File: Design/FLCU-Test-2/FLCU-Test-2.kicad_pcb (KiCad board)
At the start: 2 copper layers, 69.1 x 46.2 mm, 57 parts, among them J1 ICSP, J2 UART, J3 0348260124, U1 ATmega328-AU, U2 ULN2003ADR, U3 MCP2515-xST, U4 TJR1443, U5 NCV4276B, Y1 CSTNE16M0V530000R0, Y2 8MHz

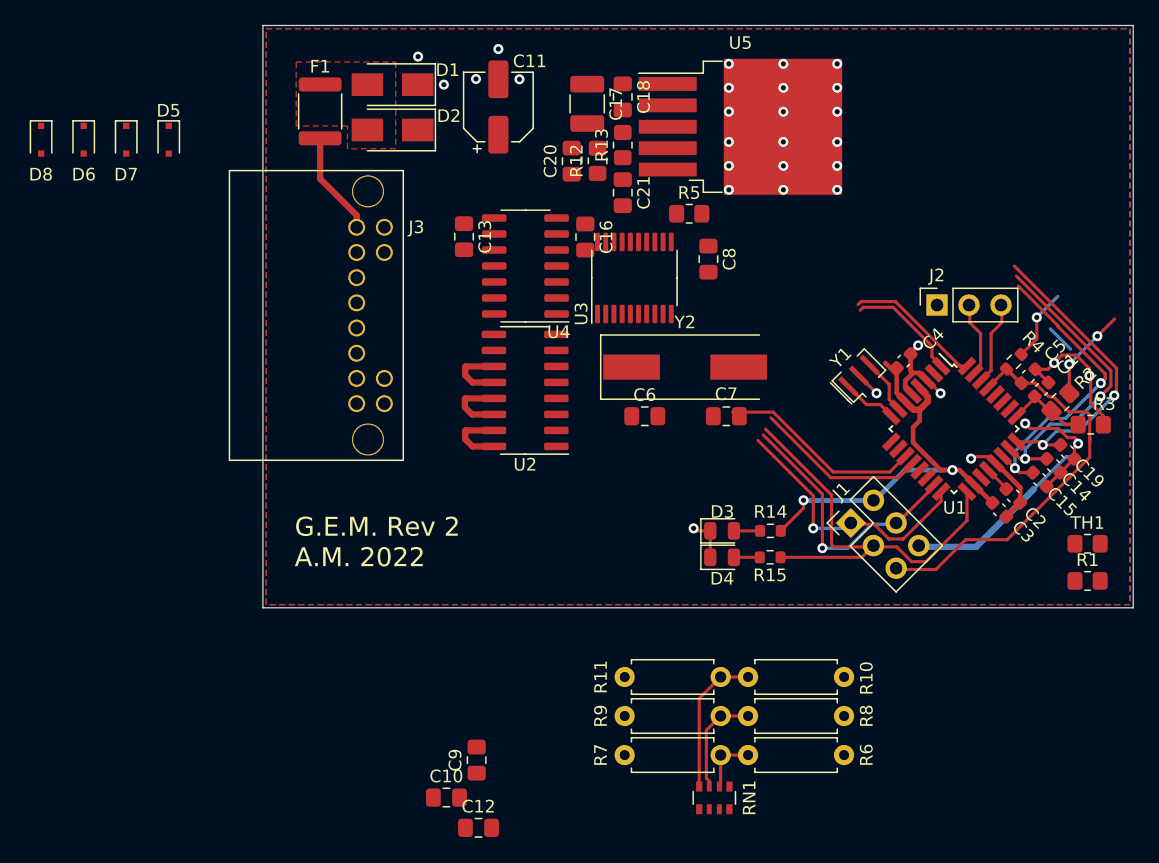
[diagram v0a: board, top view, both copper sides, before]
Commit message: Tentative Completion of Rev2 of FLCU / GEM  - Switch to TJR1443 CAN transceiver  - Smaller, more modern crystal for MCP2515  - Pulse-forming network to use sleep/wake functionality of TJR1443  - Switch from 12 to 16 pin connector to allow one additional analog input,    one digital pulse capture input, +5VOUT and signal ground  - Put CAN INT on an actual interrupt pin (lol)
This revision was done to correct some sleep/wake issues with Rev1, and to support it's use as a boost controller (with different FW)

 - Out - PWM Boost Control Solenoid
 - Out - PWM Electric Water Pump (Intercooler)
 - Out - Intercooler Fan Relay
 - DIn - Turbine speed
 - AIn - Manifold Pressure
 - AIn - Discharge Air Temperature
 - AIn - Intercooler Water Temperature
 - AIn - There was one more that I'm forgetting
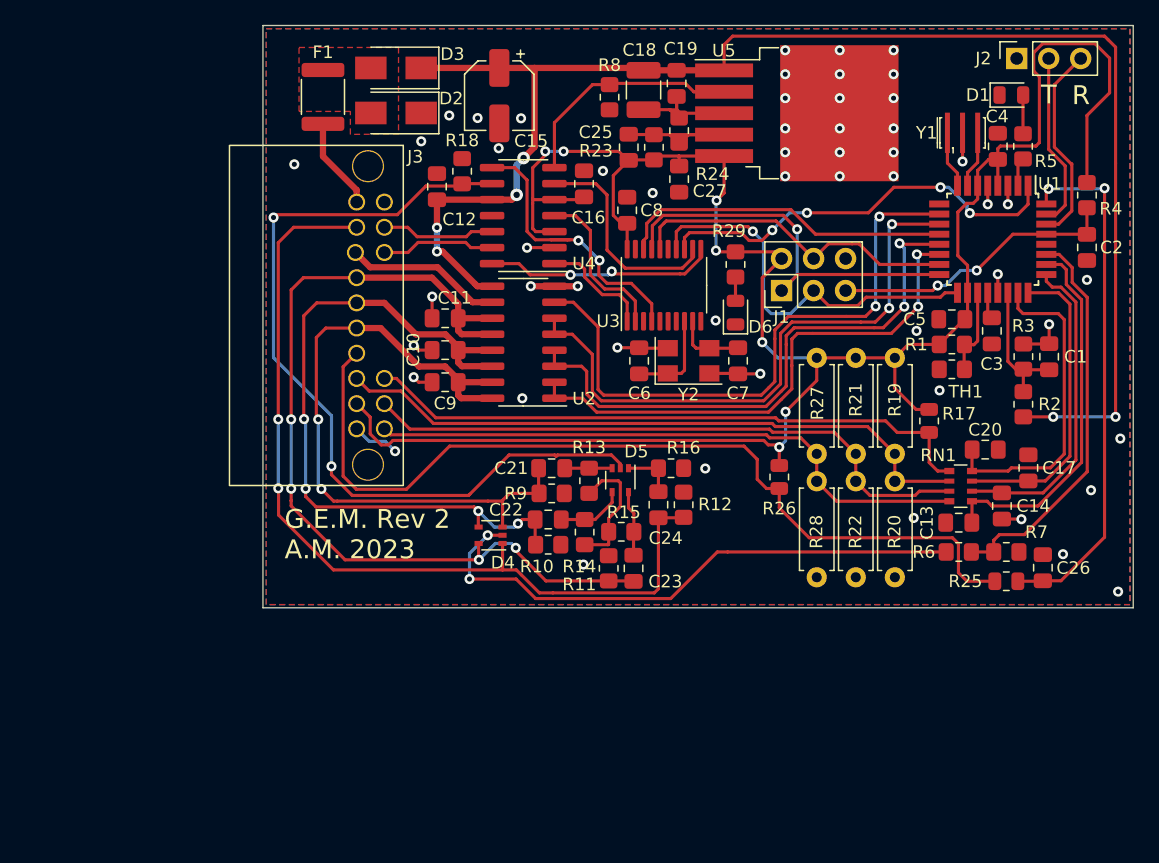
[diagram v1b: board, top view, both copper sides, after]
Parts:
- removed the C15 at (140.2, 84.1)
- removed the C19 at (142.4, 81.9)
- removed the D6 at (64.3, 57.1)
- removed D7, D8: 1N4148WS, Diode_SMD:D_SOD-323F
- added C13: 100nF, Capacitor_SMD:C_0805_2012Metric_Pad1.18x1.45mm_HandSolder, F.Cu at (133.7, 87.5)
- added C17: 100nF, Capacitor_SMD:C_0805_2012Metric_Pad1.18x1.45mm_HandSolder, F.Cu at (139.2, 83.1)
- added C20: 100nF, Capacitor_SMD:C_0805_2012Metric_Pad1.18x1.45mm_HandSolder, F.Cu at (135.8, 81.7)
- added C21: 100n, Capacitor_SMD:C_0805_2012Metric_Pad1.18x1.45mm_HandSolder, F.Cu at (101.4, 83.2)
- added C22: 100n, Capacitor_SMD:C_0805_2012Metric_Pad1.18x1.45mm_HandSolder, F.Cu at (101.1, 87.2)
- added C23: 100n, Capacitor_SMD:C_0805_2012Metric_Pad1.18x1.45mm_HandSolder, F.Cu at (107.9, 91.1)
- added C24: 100n, Capacitor_SMD:C_0805_2012Metric_Pad1.18x1.45mm_HandSolder, F.Cu at (109.9, 86.0)
- added C26: 100nF, Capacitor_SMD:C_0805_2012Metric_Pad1.18x1.45mm_HandSolder, F.Cu at (140.4, 91.0)
- added D4: MMBD4448HCQW, Package_TO_SOT_SMD:SOT-353_SC-70-5, F.Cu at (96.6, 88.5)
- added R10: 10k, Resistor_SMD:R_0805_2012Metric_Pad1.20x1.40mm_HandSolder, F.Cu at (101.1, 89.2)
- added R11: 10k, Resistor_SMD:R_0805_2012Metric_Pad1.20x1.40mm_HandSolder, F.Cu at (105.9, 91.1)
- added R12: 10k, Resistor_SMD:R_0805_2012Metric_Pad1.20x1.40mm_HandSolder, F.Cu at (111.9, 86.0)
- added R13: 10k, Resistor_SMD:R_0805_2012Metric_Pad1.20x1.40mm_HandSolder, F.Cu at (104.4, 84.2)
- added R14: 10k, Resistor_SMD:R_0805_2012Metric_Pad1.20x1.40mm_HandSolder, F.Cu at (104.0, 88.2)
- added R15: 10k, Resistor_SMD:R_0805_2012Metric_Pad1.20x1.40mm_HandSolder, F.Cu at (106.9, 88.2)
- added R16: 10k, Resistor_SMD:R_0805_2012Metric_Pad1.20x1.40mm_HandSolder, F.Cu at (110.9, 83.2)
- added R17: R, Resistor_SMD:R_0805_2012Metric, F.Cu at (131.4, 79.4)
- added R18: 10k, Resistor_SMD:R_0805_2012Metric_Pad1.20x1.40mm_HandSolder, F.Cu at (94.3, 59.6)
- added R25: 47k, Resistor_SMD:R_0805_2012Metric, F.Cu at (137.5, 92.1)
- added R26: 10k, Resistor_SMD:R_0805_2012Metric, F.Cu at (119.5, 83.8)
- added R6: 10k, Resistor_SMD:R_0805_2012Metric_Pad1.20x1.40mm_HandSolder, F.Cu at (133.7, 89.8)
- added R7: 10k, Resistor_SMD:R_0805_2012Metric_Pad1.20x1.40mm_HandSolder, F.Cu at (137.5, 89.8)
- added R9: 10k, Resistor_SMD:R_0805_2012Metric_Pad1.20x1.40mm_HandSolder, F.Cu at (101.4, 85.2)
- C1, C14, C2, C4: footprint Capacitor_SMD:C_0603_1608Metric -> Capacitor_SMD:C_0805_2012Metric_Pad1.18x1.45mm_HandSolder
- C3: value 1uF -> 100nF; footprint Capacitor_SMD:C_0603_1608Metric -> Capacitor_SMD:C_0805_2012Metric_Pad1.18x1.45mm_HandSolder
- C5: value 100nF -> 1uF; footprint Capacitor_SMD:C_0603_1608Metric -> Capacitor_SMD:C_0805_2012Metric_Pad1.18x1.45mm_HandSolder
- D5: value 1N4148WS -> MMBD4448HCQW; footprint Diode_SMD:D_SOD-323F -> Package_TO_SOT_SMD:SOT-353_SC-70-5
- J3: value 0348260124 -> 0348260160; footprint Molex_34826:0348260120 -> Molex_34826:0348260160
- R29: renamed from R14; footprint Resistor_SMD:R_0603_1608Metric -> Resistor_SMD:R_0805_2012Metric_Pad1.20x1.40mm_HandSolder
- R4: value R -> 10k; footprint Resistor_SMD:R_0603_1608Metric -> Resistor_SMD:R_0805_2012Metric_Pad1.20x1.40mm_HandSolder
- R5: renamed from R15; footprint Resistor_SMD:R_0603_1608Metric -> Resistor_SMD:R_0805_2012Metric_Pad1.20x1.40mm_HandSolder
- Y1: value CSTNE16M0V530000R0 -> 16MHz; footprint Crystal:Resonator_SMD_muRata_CSTxExxV-3Pin_3.0x1.1mm -> Crystal:Resonator_SMD_Murata_CSTxExxV-3Pin_3.0x1.1mm_HandSoldering
- Y2: footprint Crystal:Crystal_SMD_HC49-SD -> Crystal:Crystal_SMD_5032-4Pin_5.0x3.2mm
- moved D5 44.9 mm to (106.9, 84.1)
- moved D1 43.3 mm to (137.9, 53.5)
- moved C11 40.5 mm to (93.0, 71.2), turned to 180 degrees
- moved R5 38.3 mm to (138.8, 57.6), turned to 90 degrees
- moved C10 35.5 mm to (93.0, 73.8), turned to 180 degrees
- moved R19 31.8 mm to (128.7, 74.4), turned to -90 degrees
- moved RN1 31.5 mm to (133.9, 84.6), turned to 0 degrees
- moved C9 30.1 mm to (93.0, 76.3), turned to 180 degrees
- moved R21 28.5 mm to (125.5, 74.4), turned to -90 degrees
- moved R20 25.8 mm to (128.7, 84.2), turned to -90 degrees
- moved R27 25.4 mm to (122.5, 74.4), turned to -90 degrees
- moved R1 21.6 mm to (133.2, 73.3)
- moved R22 21.5 mm to (125.5, 84.2), turned to -90 degrees
- moved R29 21.3 mm to (116.0, 67.0), turned to -90 degrees
- moved Y1 21.0 mm to (134.0, 56.5), turned to 0 degrees
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- renumbered C12 to C11, C16 to C12, C11 to C15, C13 to C16, C17 to C18, C18 to C19, C20 to C25, C21 to C27, D4 to D1, D1 to D2, D2 to D3, D3 to D6, R6 to R19, R7 to R20, R8 to R21, R9 to R22, R12 to R23, R13 to R24, R10 to R27, R11 to R28, R5 to R8
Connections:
- C10 pad 1: Main-Level-Out -> /Main-Level-Out
- C11 pad 1: Low-Level-Warning-Out -> /Low-Level-Warning-Out
- C2 pad 1: Net-(C2-Pad1) -> GND
- C2 pad 2: GND -> RESET
- C3 pad 1: GND -> Net-(C3-Pad1)
- C3 pad 2: +5V -> GND
- C4 pad 1: +5V -> GND
- C4 pad 2: GND -> +5V
- C5 pad 1: GND -> +5V
- C5 pad 2: RESET -> GND
- C9 pad 1: Sub-Level-Out -> /Sub-Level-Out
- D2 pad 2: Net-(D1-Pad2) (its old number) -> /POSTFUSE
- D3 pad 2: Net-(D1-Pad2) (its old number) -> /POSTFUSE
- D5 pad 1: unconnected-(D5-Pad1) -> Net-(D5-Pad1)
- D5 pad 2: Sub-Level-Out -> /Wake_Pulse
- F1 pad 1: Net-(D1-Pad2) (its old number) -> /POSTFUSE
- J3 pad 10: Sub-Level-Out -> /Low-Level-Warning-Out
- J3 pad 11: /Extra-Out -> /Main-Level-Out
- J3 pad 12: Low-Level-Warning-In -> /Sub-Level-Out
- J3 pad 3: Sub-Level-In -> CAN_H
- J3 pad 4: Main-Level-In -> /A4_In
- J3 pad 5: +12V_BATTERY -> /A2_In
- J3 pad 6: CAN_H -> /A1_In
- J3 pad 7: +12V_IGN -> +12V_BATTERY
- J3 pad 8: Low-Level-Warning-Out -> +12V_IGN
- J3 pad 9: Main-Level-Out -> /Extra-Out
- R19 pad 1: Net-(R10-Pad1) -> +5V
- R19 pad 2: Low-Level-Warning-In -> /A3_In
- R20 pad 1: Low-Level-Warning-In -> /A3_In
- R21 pad 1: Net-(R10-Pad1) -> +5V
- R21 pad 2: Sub-Level-In -> /A2_In
- R22 pad 1: Sub-Level-In -> /A2_In
- R27 pad 1: Net-(R10-Pad1) -> +5V
- R27 pad 2: Main-Level-In -> /A1_In
- R28 pad 1: Main-Level-In -> /A1_In
- R5 pad 1: SCK -> Net-(R5-Pad1)
- RN1 pad 1: VReg_EN -> /A4_In
- RN1 pad 2: Low-Level-Warning-In -> /A3_In
- RN1 pad 3: Sub-Level-In -> /A2_In
- RN1 pad 4: Main-Level-In -> /A1_In
- RN1 pad 8: GND -> /Spare-Analog
- U1 pad 1: Net-(U1-Pad1) -> CAN_INT
- U1 pad 10: Net-(U1-Pad10) -> /D4
- U1 pad 11: CAN_INT -> /PWM2
- U1 pad 13: unconnected-(U1-Pad13) -> /PWM1
- U1 pad 14: unconnected-(U1-Pad14) -> /PWM3
- U1 pad 2: unconnected-(U1-Pad2) -> Net-(R5-Pad1)
- U1 pad 20: Net-(C2-Pad1) -> Net-(C3-Pad1)
- U1 pad 23: Sub-Level -> /Spare-Analog
- U1 pad 25: Module-Voltage -> Sub-Level
- U1 pad 26: unconnected-(U1-Pad26) -> Main-Lvl
- U1 pad 27: unconnected-(U1-Pad27) -> /Wake_Sense
- U1 pad 32: Net-(U1-Pad32) -> EXT_INT
- U1 pad 9: Net-(U1-Pad9) -> unconnected-(U1-Pad9)
- U2 pad 1: Net-(U1-Pad10) -> /PWM3
- U2 pad 11: Low-Level-Warning-Out -> /Low-Level-Warning-Out
- U2 pad 12: Low-Level-Warning-Out -> /Low-Level-Warning-Out
- U2 pad 13: Main-Level-Out -> /Main-Level-Out
- U2 pad 14: Main-Level-Out -> /Main-Level-Out
- U2 pad 15: Sub-Level-Out -> /Sub-Level-Out
- U2 pad 16: Sub-Level-Out -> /Sub-Level-Out
- U2 pad 2: Net-(U1-Pad10) -> /PWM3
- U2 pad 3: Net-(U1-Pad9) -> /PWM1
- U2 pad 4: Net-(U1-Pad9) -> /PWM1
- U2 pad 5: Net-(U1-Pad1) -> /PWM2
- U2 pad 6: Net-(U1-Pad1) -> /PWM2
- U2 pad 7: Net-(U1-Pad32) -> /D4
- U4 pad 10: +5V -> +12V
- U4 pad 5: +12V -> +5V
- U4 pad 9: /WAKE -> /Wake_Pulse
- Y2 pad 2: Net-(C7-Pad1) -> GND
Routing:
- net +5V: track 43.8 -> 172.6 mm, vias 3 -> 7
- net +12V: track 7.39 -> 127.7 mm, vias 2 -> 6
- net /Low-Level-Warning-Out: track 0.00 -> 71.7 mm, vias 0 -> 4
- net /D1_INT_In: track 0.00 -> 71.4 mm
- net +12V_IGN: track 0.00 -> 71.0 mm, vias 0 -> 2
- net /Wake_Pulse: track 0.00 -> 66.5 mm, vias 0 -> 2
- net /Main-Level-Out: track 0.00 -> 58.1 mm, vias 0 -> 4
- net /Sub-Level-Out: track 0.00 -> 54.3 mm, vias 0 -> 2
- net /A3_In: track 0.00 -> 51.7 mm
- net /A4_In: track 0.00 -> 49.3 mm
- net /A2_In: track 0.00 -> 49.3 mm
- net /D4: track 0.00 -> 48.9 mm, vias 0 -> 2
- net /A1_In: track 0.00 -> 48.5 mm
- net /PWM2: track 0.00 -> 47.7 mm, vias 0 -> 2
- net /PWM1: track 0.00 -> 45.4 mm, vias 0 -> 2
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- added copper zone on F.Cu, net /POSTFUSE
- removed copper zone on F.Cu, net Net-(D1-Pad2) (its old number)
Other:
- board text added: "G.E.M. Rev 2 A.M. 2023"
- board text added: "R"
- board text added: "T"
- board text removed: "G.E.M. Rev 2 A.M. 2022"

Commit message: GEM Rev2 (formerly FLCU Rev2) design & layout complete.
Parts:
- renumbered U2 to U3, U3 to U4, U4 to U5, U5 to U6
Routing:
- net GND: vias 53 -> 63
